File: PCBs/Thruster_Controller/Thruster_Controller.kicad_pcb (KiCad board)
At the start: 4 copper layers, 36 x 37.5 mm, 110 parts, among them J1 PHASE_A, J2 PHASE_B, J3 PHASE_C, J5 Pogo Conn, J7 Conn_01x01, J8 Conn_01x01, Q1 SIZF906DT, Q2 SIZF906DT, Q3 SIZF906DT, U1 DRV8305, U2 RTQ2569-50GQW, U3 MCP2515, U4 TPS62172DSGR, U5 TMS320F28027F, U8 MCP2562, Y1 20MHz

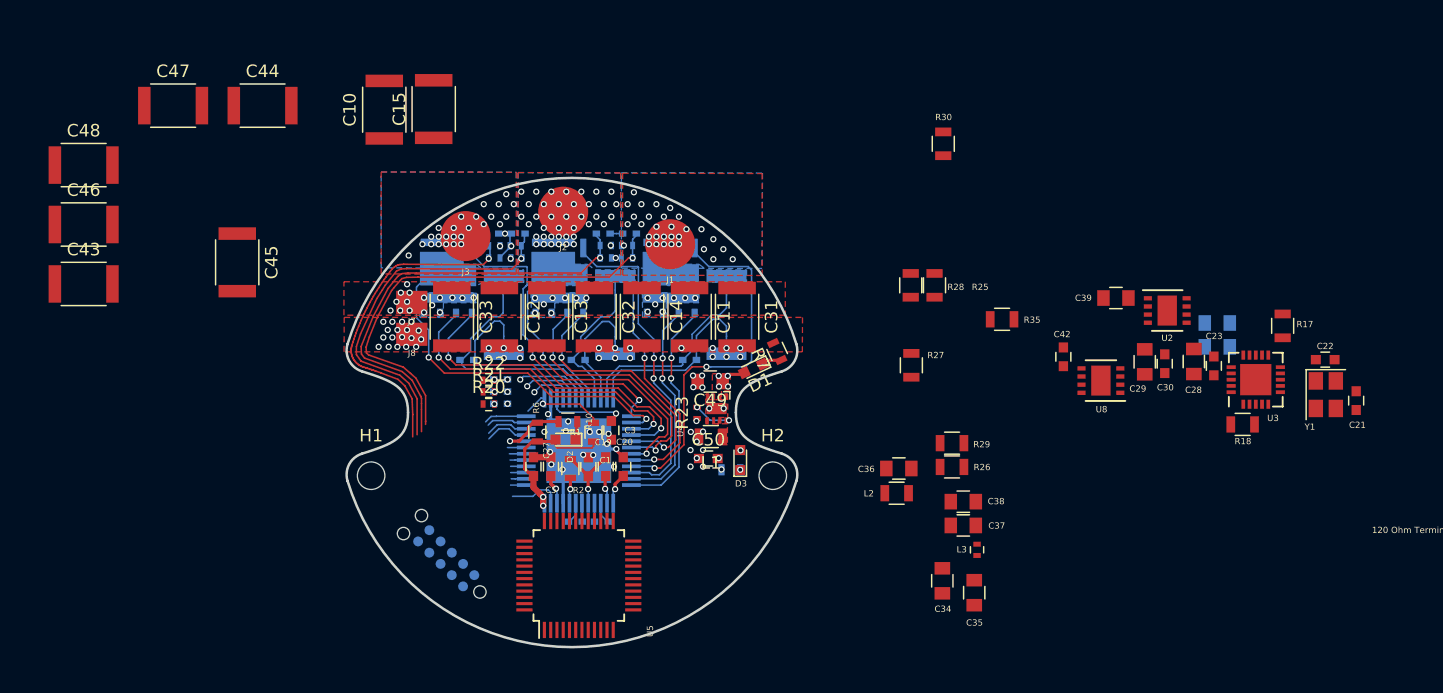
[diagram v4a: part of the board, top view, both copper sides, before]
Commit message: Initial Routing Finished
- All layout and routing initially finished
- Still need to clean up silkscreen and any routing blemishes
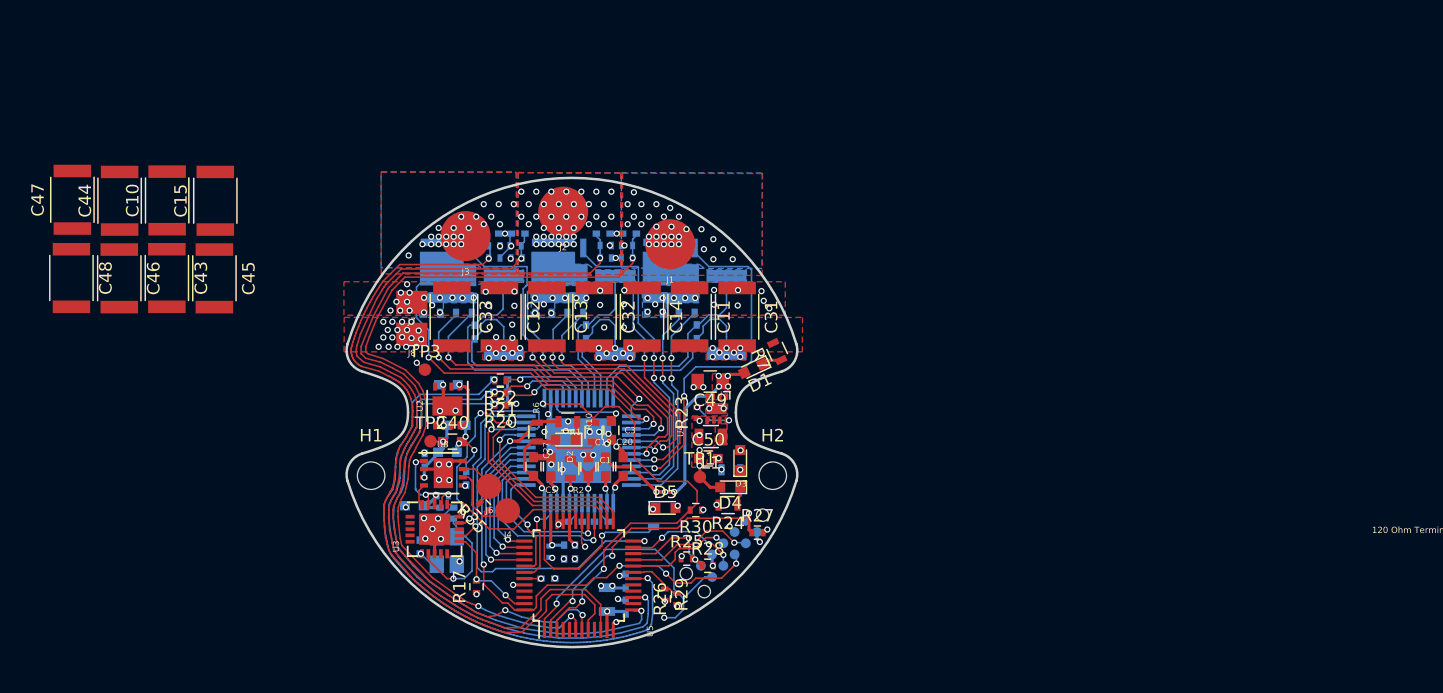
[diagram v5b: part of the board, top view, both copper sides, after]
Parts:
- added D4: RED, LEDs:LED_0603, F.Cu at (112.1, 105.4)
- added D5: Orange, LEDs:LED_0603, F.Cu at (106.9, 107.1)
- added J4: Conn_01x01, Thruster_Controller:CAN_Pad, F.Cu at (94.3, 107.3)
- added J6: Conn_01x01, Thruster_Controller:CAN_Pad, F.Cu at (92.8, 105.3)
- added R24: 680, Resistors_SMD:R_0603, F.Cu at (111.9, 106.8)
- added R31: 680, Resistors_SMD:R_0603, B.Cu at (106.0, 107.8)
- added TP1: TestPoint, Thruster_Controller:TestPoint_Pad_D1.0mm, F.Cu at (109.7, 104.6)
- added TP2: TestPoint, Thruster_Controller:TestPoint_Pad_D1.0mm, F.Cu at (88.2, 101.8)
- added TP3: TestPoint, Thruster_Controller:TestPoint_Pad_D1.0mm, F.Cu at (87.7, 96.0)
- C21, C22, C23, C30, C42: footprint Capacitors_SMD:C_0603 -> Capacitors_SMD:C_0402; moved to B.Cu
- C28, C29, C39: footprint Capacitors_SMD:C_0805 -> Capacitors_SMD:C_0603; moved to B.Cu
- C34, C35, C36, C37, C38: footprint Capacitors_SMD:C_0805 -> Capacitors_SMD:C_0402; moved to B.Cu
- C40: footprint Capacitors_SMD:C_0805 -> Capacitors_SMD:C_0603; moved to F.Cu
- C41: footprint Capacitors_SMD:C_0805 -> Capacitors_SMD:C_0603
- L2, L3, Y1: moved to B.Cu
- R17, R25, R26, R27, R28, R29, R30, R35: footprint Resistors_SMD:R_0805 -> Resistors_SMD:R_0402
- R18: footprint Resistors_SMD:R_0805 -> Resistors_SMD:R_0402; moved to B.Cu
- moved C21 75.8 mm to (87.3, 110.2)
- moved C22 71.4 mm to (89.4, 107.9), turned to 180 degrees
- moved Y1 71.3 mm to (89.5, 110.5)
- moved R17 67.7 mm to (91.8, 113.4), turned to 90 degrees
- moved U3 66.7 mm to (88.5, 108.8), turned to 0 degrees
- moved R18 64.2 mm to (89.1, 106.1), turned to 0 degrees
- moved C28 63.4 mm to (86.8, 106.9), turned to 180 degrees
- moved C23 62.3 mm to (89.5, 107.0), turned to 0 degrees
- moved C40 61.6 mm to (89.9, 101.8)
- moved C41 61.4 mm to (90.2, 100.5)
- moved C30 59.7 mm to (87.7, 103.3)
- moved U2 58.0 mm to (89.5, 98.9), turned to 270 degrees
- moved C29 56.2 mm to (89.5, 102.6), turned to 0 degrees
- moved C39 53.8 mm to (89.6, 97.2)
- moved U8 53.1 mm to (89.2, 104.3), turned to 0 degrees
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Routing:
- net /TI_MCU/ADCINB7: track 0.06 -> 48.5 mm, vias 1 -> 2
- net /TI_MCU/ADCINB3: track 0.24 -> 44.9 mm, vias 1 -> 2
- net /TI_MCU/ADCINB1: track 0.06 -> 41.1 mm, vias 1 -> 2
- net /GPIO28: track 6.02 -> 44.1 mm, vias 1 -> 5
- net /TI_MCU/ADCINA1: track 27.1 -> 59.6 mm
- net /TI_MCU/ADCINA0: track 29.2 -> 61.7 mm
- net GND: track 30.7 -> 60.7 mm, vias 66 -> 105
- net /Powertrain/SPI_MOSI: track 3.42 -> 33.2 mm, vias 0 -> 2
- net /Powertrain/PWRGD: track 7.20 -> 36.8 mm, vias 1 -> 3
- net /Powertrain/SPI_CLK: track 3.44 -> 32.4 mm, vias 0 -> 2
- net /TI_MCU/ADCINA3: track 34.7 -> 63.6 mm, vias 1 -> 3
- net /TI_MCU/ADCINA7: track 36.3 -> 63.9 mm, vias 1 -> 3
- net /Powertrain/SPI_MISO: track 3.26 -> 28.6 mm, vias 0 -> 3
- net +BATT: track 8.33 -> 32.9 mm, vias 38 -> 58
- net /TRST: track 0.00 -> 23.5 mm, vias 0 -> 3
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- added copper zone on F.Cu, net +3V3

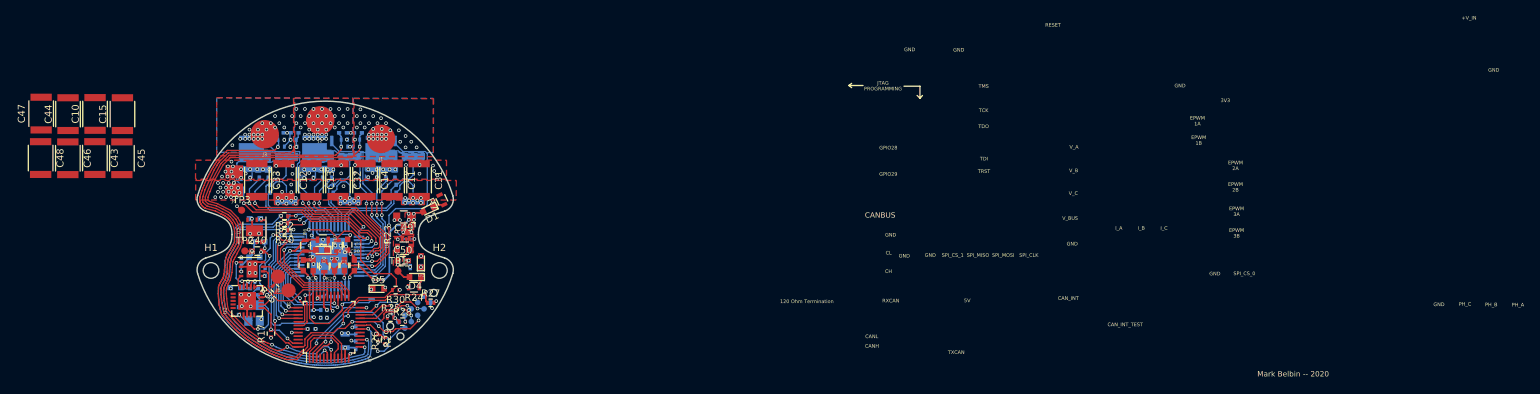
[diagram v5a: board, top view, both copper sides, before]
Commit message: Silk and Routing
- Fixed 5V LED indicator
- Small layout and routing cleanups
- Cleaned up Silkscreen
- Board is "finished" !!
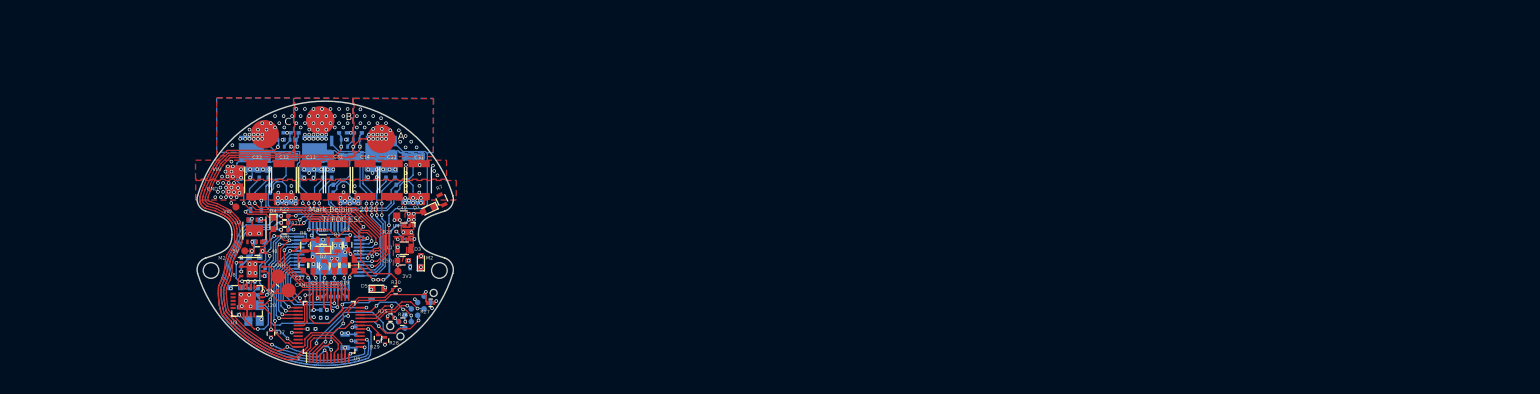
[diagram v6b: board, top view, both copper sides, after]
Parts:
- removed C10, C15, C43, C44, C45, C46, C47, C48: 22uF, Capacitors_SMD:C_1812
- R24: moved to B.Cu
- moved R24 24.7 mm to (89.7, 96.0), turned to 0 degrees
- moved D4 21.3 mm to (92.2, 97.9), turned to 270 degrees
- moved R5 1.00 mm to (103.9, 87.1)
- moved R14 1.00 mm to (103.8, 86.1)
- moved TP3 0.92 mm to (86.9, 95.6)
- moved C39 0.20 mm to (89.6, 97.4)
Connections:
- D4 pad 2: +3V3 -> +5V
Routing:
- net +5V: track 5.99 -> 11.2 mm
- net /GPIO29: track 23.0 -> 18.9 mm, vias 2 -> 1
- net Net-(D4-Pad1): track 1.52 -> 5.11 mm, vias 0 -> 1
- net /Powertrain/Phase_A: track 0.00 -> 2.68 mm
- net GND: track 60.7 -> 63.2 mm, vias 105 -> 108
- net +3V3: track 21.7 -> 19.7 mm
- net /TI_MCU/ADCINB7: track 48.5 -> 47.5 mm
- net /TI_MCU/ADCINB3: track 44.9 -> 43.9 mm
- net /TI_MCU/ADCINB1: track 41.1 -> 40.2 mm
- net +BATT: track 32.9 -> 32.8 mm, vias 58 -> 50
- added copper zone on In1.Cu, net +BATT
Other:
- board text added: "1"
- board text added: "120"
- board text added: "A"
- board text added: "B"
- board text added: "C"
- board text added: "M2"
- board text added: "Mark Belbin - 2020"
- board text added: "TI FOC ESC"
- board text added: "VIN"
- board text removed: "+V_IN"
- board text removed: "120 Ohm Termination"
- board text removed: "CANBUS"
- board text removed: "CAN_INT"
- board text removed: "CAN_INT_TEST"
- board text removed: "CH"
- board text removed: "CL"
- board text removed: "EPWM 1A"
- board text removed: "EPWM 1B"
- board text removed: "EPWM 2A"
- board text removed: "EPWM 2B"
- board text removed: "EPWM 3A"
- board text removed: "EPWM 3B"
- board text removed: "GPIO28"
- board text removed: "GPIO29"
- board text removed: "I_A"
- board text removed: "I_B"
- board text removed: "I_C"
- board text removed: "Mark Belbin -- 2020"
- board text removed: "PH_A"
- board text removed: "PH_B"
- board text removed: "PH_C"
- board text removed: "RESET"
- board text removed: "RXCAN"
- board text removed: "SPI_CLK"
- board text removed: "SPI_CS_0"
- board text removed: "SPI_CS_1"
- board text removed: "SPI_MISO"
- board text removed: "SPI_MOSI"
- board text removed: "TCK"
- board text removed: "TDI"
- board text removed: "TDO"
- board text removed: "TMS"
- board text removed: "TRST"
- board text removed: "TXCAN"
- board text removed: "V_A"
- board text removed: "V_B"
- board text removed: "V_BUS"
- board text removed: "V_C"

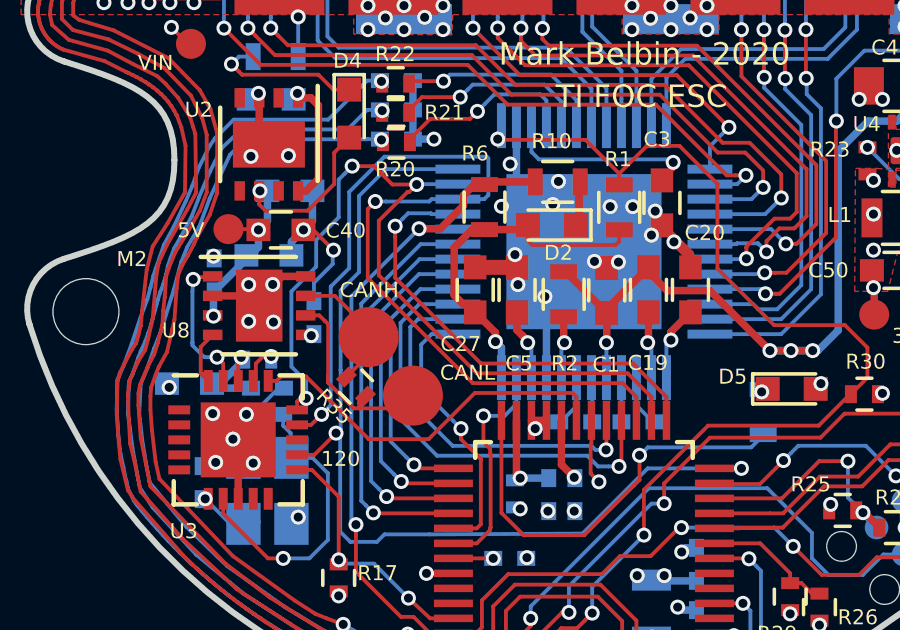
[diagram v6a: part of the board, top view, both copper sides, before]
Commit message: BOM and Small Changes
- Created BOM
- Small routing cleanups
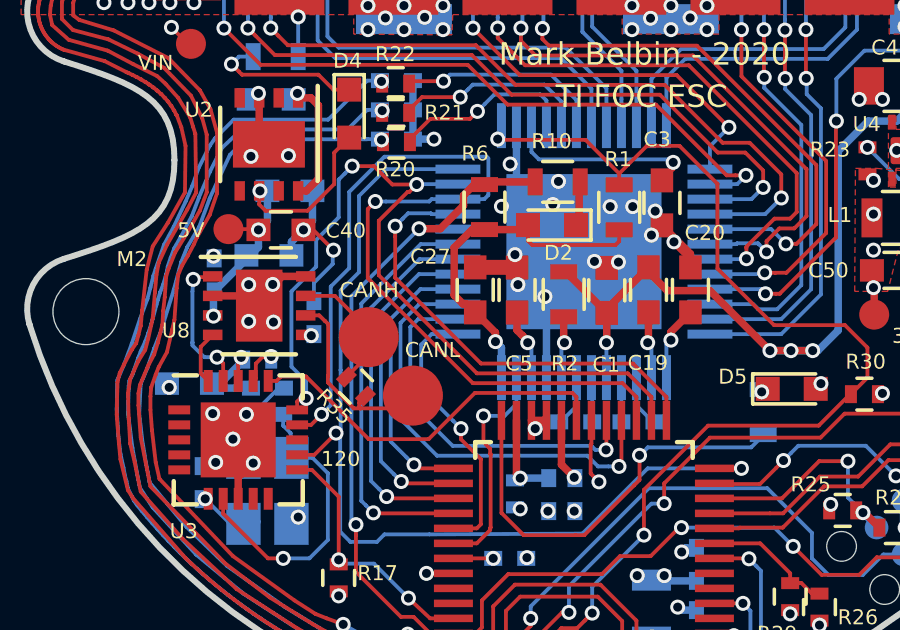
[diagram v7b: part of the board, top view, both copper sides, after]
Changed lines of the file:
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@@
   (layers
     (0 F.Cu signal)
-    (1 In1.Cu power)
-    (2 In2.Cu power)
+    (1 In1.Cu power hide)
+    (2 In2.Cu power hide)
     (31 B.Cu signal)
     (32 B.Adhes user)
@@
     (tags "capacitor 0603")
     (attr smd)
-    (fp_text reference C27 (at -1.805 -0.485 180) (layer F.SilkS)
+    (fp_text reference C27 (at 1.105 -1.495 180) (layer F.SilkS)
       (effects (font (size 0.5 0.5) (thickness 0.125)))
     )
@@
     (effects (font (size 0.5 0.5) (thickness 0.125)))
   )
-  (gr_text CANL (at 96.12 106.54) (layer F.SilkS)
+  (gr_text CANL (at 94.95 105.78) (layer F.SilkS)
     (effects (font (size 0.5 0.5) (thickness 0.125)))
   )

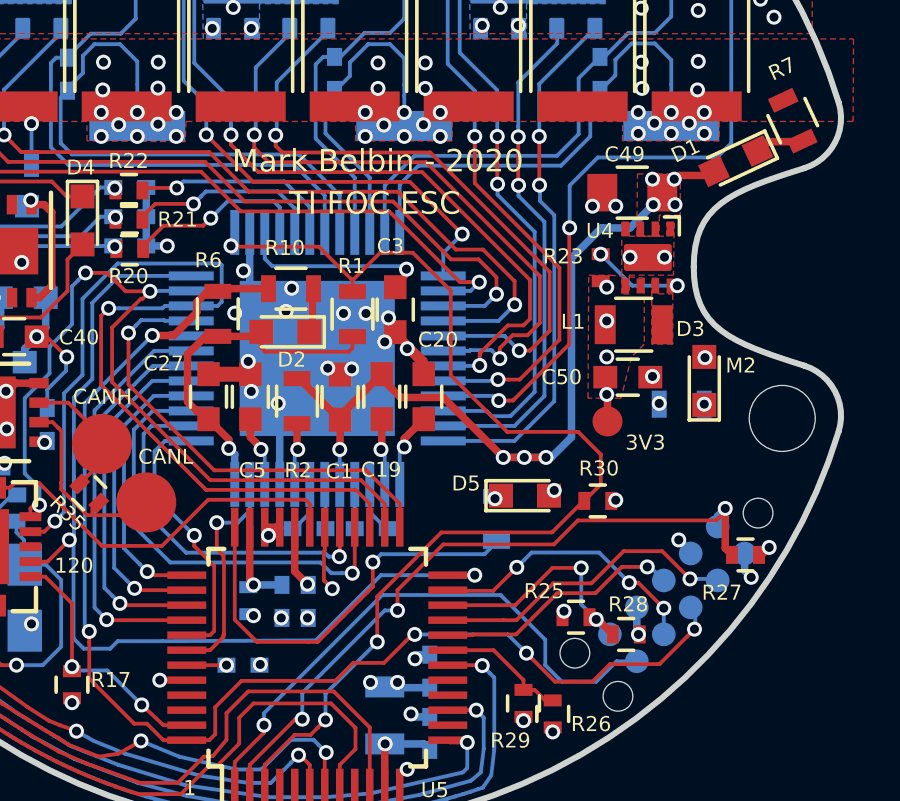
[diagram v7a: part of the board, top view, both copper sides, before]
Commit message: BOM Changes
- Found cheaper alternatives for some components
- Changed sizing of some components to reduce cost where possible
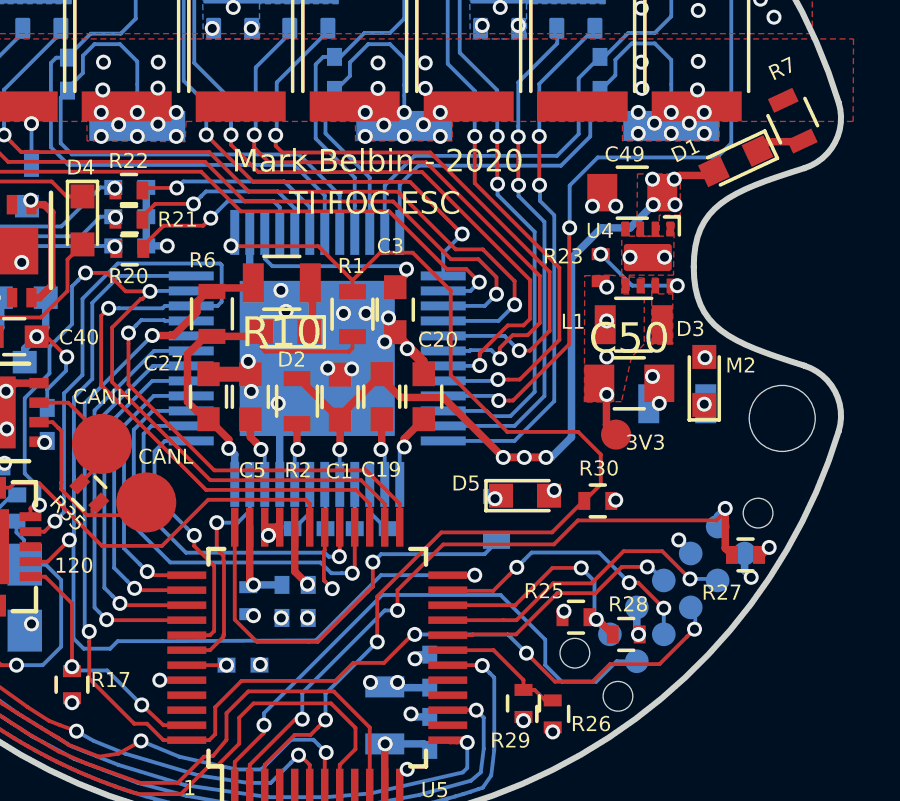
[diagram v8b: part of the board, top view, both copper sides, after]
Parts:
- C50: footprint Capacitors_SMD:C_0603 -> Capacitors_SMD:C_0805
- R10, R19: footprint Resistors_SMD:R_0603 -> Resistors_SMD:R_0805
- R11, R8, R9: footprint MCU_Powertrain:R_2512_Sense -> Resistors_SMD:R_2512
- moved TP1 0.52 mm to (110.0, 105.0)
- moved R10 0.36 mm to (98.8, 100.0)
- moved C50 0.21 mm to (110.4, 103.3)
- moved R6 0.20 mm to (96.5, 101.0)
- moved R19 0.15 mm to (112.0, 104.0)
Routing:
- net +3V3: track 19.7 -> 20.3 mm
- net GND: vias 108 -> 106
